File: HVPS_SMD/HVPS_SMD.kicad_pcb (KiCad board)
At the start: 2 copper layers, 30 x 20 mm, 25 parts, among them J1 CONN_01X02, J2 CONN_01X02, J3 CONN_01X02, Q1 AO4294, T1 MagTop-HVSMPS, U1 3478

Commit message: Title blocks
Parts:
- moved Cs1 47.3 mm to (147.7, 97.7)
- moved FID1 47.3 mm to (162.2, 104.8)
- moved J3 47.3 mm to (152.7, 106.7)
- moved R2 47.3 mm to (149.0, 105.1)
- moved Rs2 47.3 mm to (138.5, 97.8)
- moved U1 47.3 mm to (144.5, 103.3)
- moved C1 47.3 mm to (159.6, 104.8)
- moved Cc1 47.3 mm to (140.0, 103.0)
- moved FID4 47.3 mm to (136.6, 106.6)
- moved R3 47.3 mm to (136.6, 101.0)
- moved Rc1 47.3 mm to (136.6, 103.0)
- moved Rs1 47.3 mm to (147.7, 93.8)
- moved C3 47.3 mm to (139.5, 91.3)
- moved D1 47.3 mm to (144.7, 89.8)
- moved FID3 47.3 mm to (150.3, 95.2)
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
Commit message: Documentation
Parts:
- moved G*** 47.3 mm to (150.4, 96.0)
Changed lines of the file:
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@@
     (solder_mask_min_width 0.25)
     (pad_to_paste_clearance -0.04)
+    (aux_axis_origin 134.97 108.11)
+    (grid_origin 134.97 108.11)
     (pcbplotparams
-      (layerselection 0x0020000_7ffffffe)
+      (layerselection 0x00010f8_ffffffff)
       (disableapertmacros false)
       (usegerberextensions true)
@@
       (sketchpadsonfab false)
       (subtractmaskfromsilk false)
-      (outputformat 4)
+      (outputformat 1)
       (mirror false)
       (drillshape 0)
@@
     (pad "5" smd rect (at -2.99974 -5.97408 270) (size 1.4986 2.2479) (layers "F.Cu" "F.Paste" "F.Mask")
       (net 1 "Vin") (pinfunction "5") (pintype "passive"))
-    (pad "6" smd rect (at -4.99872 -5.97408 270) (size 1.4986 2.2479) (layers "F.Cu" "F.Mask"))
-    (pad "7" smd rect (at -4.99872 5.97408 270) (size 1.4986 2.2479) (layers "F.Cu" "F.Mask"))
+    (pad "6" smd rect (at -4.99872 -5.97408 270) (size 1.4986 2.2479) (layers "F.Cu" "F.Paste" "F.Mask"))
+    (pad "7" smd rect (at -4.99872 5.97408 270) (size 1.4986 2.2479) (layers "F.Cu" "F.Paste" "F.Mask"))
     (pad "8" smd rect (at -2.99974 5.97408 270) (size 1.4986 2.2479) (layers "F.Cu" "F.Paste" "F.Mask")
       (net 14 "GND") (pinfunction "8") (pintype "passive"))
-    (pad "11" smd rect (at 2.99974 5.97408 270) (size 1.4986 2.2479) (layers "F.Cu" "F.Mask"))
-    (pad "12" smd rect (at 4.99872 5.97408 270) (size 1.4986 2.2479) (layers "F.Cu" "F.Mask"))
+    (pad "11" smd rect (at 2.99974 5.97408 270) (size 1.4986 2.2479) (layers "F.Cu" "F.Paste" "F.Mask"))
+    (pad "12" smd rect (at 4.99872 5.97408 270) (size 1.4986 2.2479) (layers "F.Cu" "F.Paste" "F.Mask"))
   )
   (footprint "NixieClockMaster:Header_MA02-Edge-3.2" (layer "F.Cu")
@@
     (property "Sheetname" "")
     (attr smd)
-    (fp_text reference "R2" (at 0 -1.651) (layer "Cmts.User")
+    (fp_text reference "R2" (at 0 -1.651) (layer "F.Fab")
       (effects (font (size 0.75 0.75) (thickness 0.1)))
     )
@@
       (effects (font (size 0.5 0.5) (thickness 0.08)))
     )
-    (fp_text user "${REFERENCE}" (at 0 0) (layer "F.Fab") hide
+    (fp_text user "C328384" (at 0 0) (layer "Cmts.User") hide
       (effects (font (size 0.5 0.5) (thickness 0.075)))
     )
@@
   )
   (footprint "NixieClockMaster:LOGO-Nixieclock-small.biz" (layer "B.Cu")
-    (at 115.405 127.915 180)
+    (at 150.375 96.005 180)
     (attr board_only exclude_from_pos_files exclude_from_bom)
     (fp_text reference "G***" (at 0 0) (layer "B.Fab")
@@
   (gr_arc (start 134.966 89.106) (mid 135.250658 88.390658) (end 135.966 88.106) (layer "Edge.Cuts") (width 0.127))
   (gr_arc (start 135.966 108.106) (mid 135.250658 107.821342) (end 134.966 107.106) (layer "Edge.Cuts") (width 0.127))
-  (gr_text "5V" (at 127.13 135.19 90) (layer "F.SilkS")
+  (gr_text "5V" (at 162.1 103.28 90) (layer "F.SilkS")
     (effects (font (size 0.6 0.6) (thickness 0.127)))
   )
-  (gr_text "Thanks to\nnixies.us\n\nwww.nixieclock.biz" (at 121.205 127.365 90) (layer "F.SilkS")
+  (gr_text "Thanks to\nnixies.us\n\nwww.nixieclock.biz" (at 156.175 95.455 90) (layer "F.SilkS")
     (effects (font (size 0.6 0.6) (thickness 0.127)))
   )
-  (gr_text "Nixie Power Supply\nv1.0 07May2024" (at 117.63 134.965) (layer "F.SilkS")
+  (gr_text "Nixie Power Supply\nv1.0 07May2024" (at 152.6 103.055) (layer "F.SilkS")
     (effects (font (size 0.6 0.6) (thickness 0.127)))
   )
-  (gr_text "GND" (at 101.23 126.99) (layer "F.SilkS")
+  (gr_text "GND" (at 136.2 95.08) (layer "F.SilkS")
     (effects (font (size 0.6 0.6) (thickness 0.127)))
   )
-  (gr_text "HV" (at 101.13 120.69) (layer "F.SilkS")
+  (gr_text "HV" (at 136.1 88.78) (layer "F.SilkS")
     (effects (font (size 0.6 0.6) (thickness 0.127)))
   )
-  (gr_text "GND" (at 127.13 138.44 90) (layer "F.SilkS")
+  (gr_text "GND" (at 162.1 106.53 90) (layer "F.SilkS")
     (effects (font (size 0.6 0.6) (thickness 0.127)))
   )

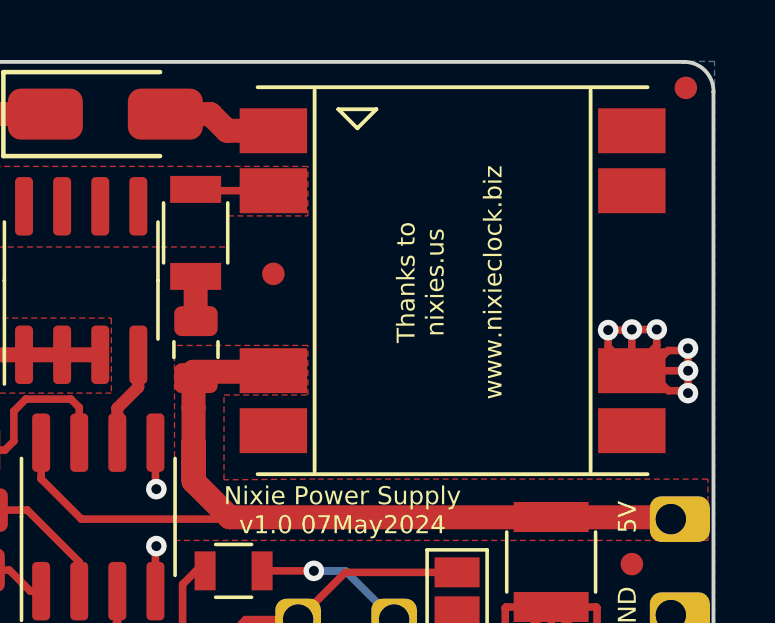
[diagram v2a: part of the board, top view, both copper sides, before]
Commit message: Update Kicad version
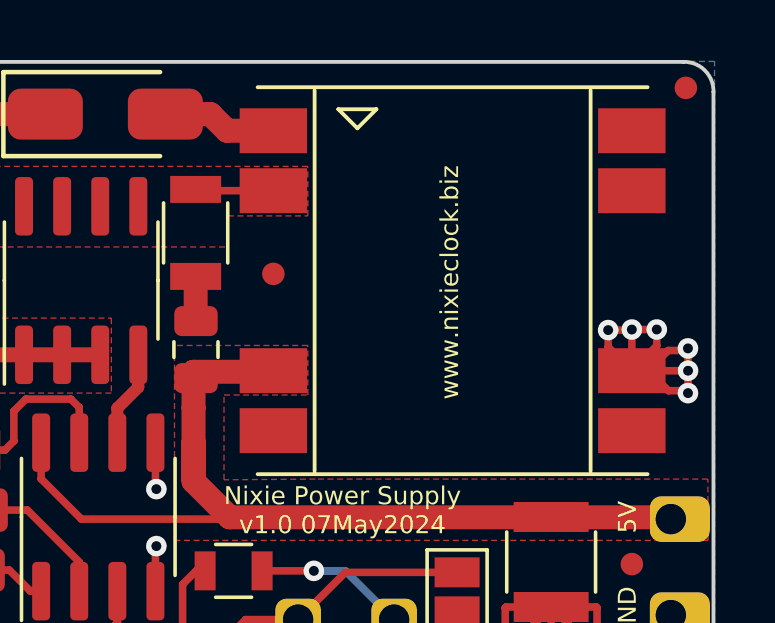
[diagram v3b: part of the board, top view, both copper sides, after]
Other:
- board text added: "www.nixieclock.biz"
- board text removed: "Thanks to nixies.us www.nixieclock.biz"
